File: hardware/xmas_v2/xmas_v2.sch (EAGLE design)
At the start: 30 parts

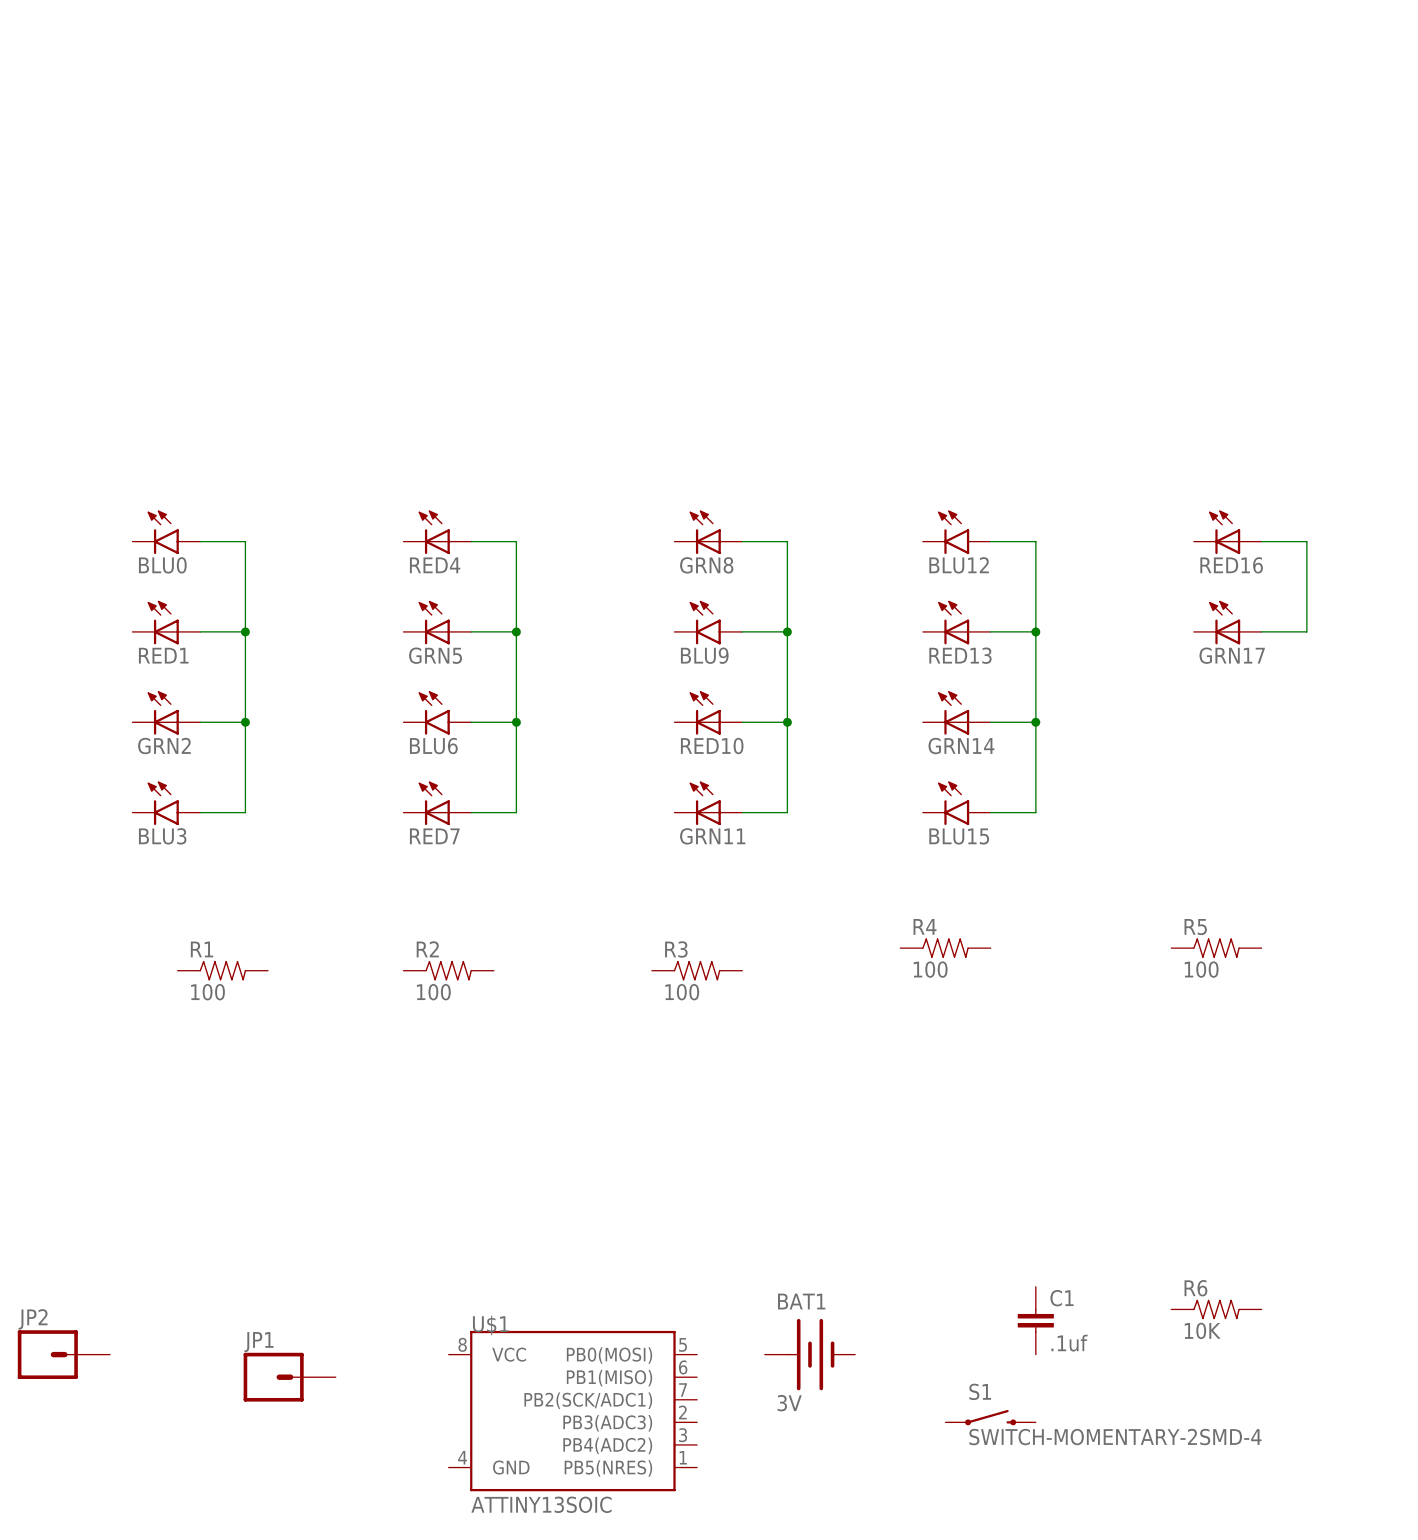
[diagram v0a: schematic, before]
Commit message: Added charlieplex schem
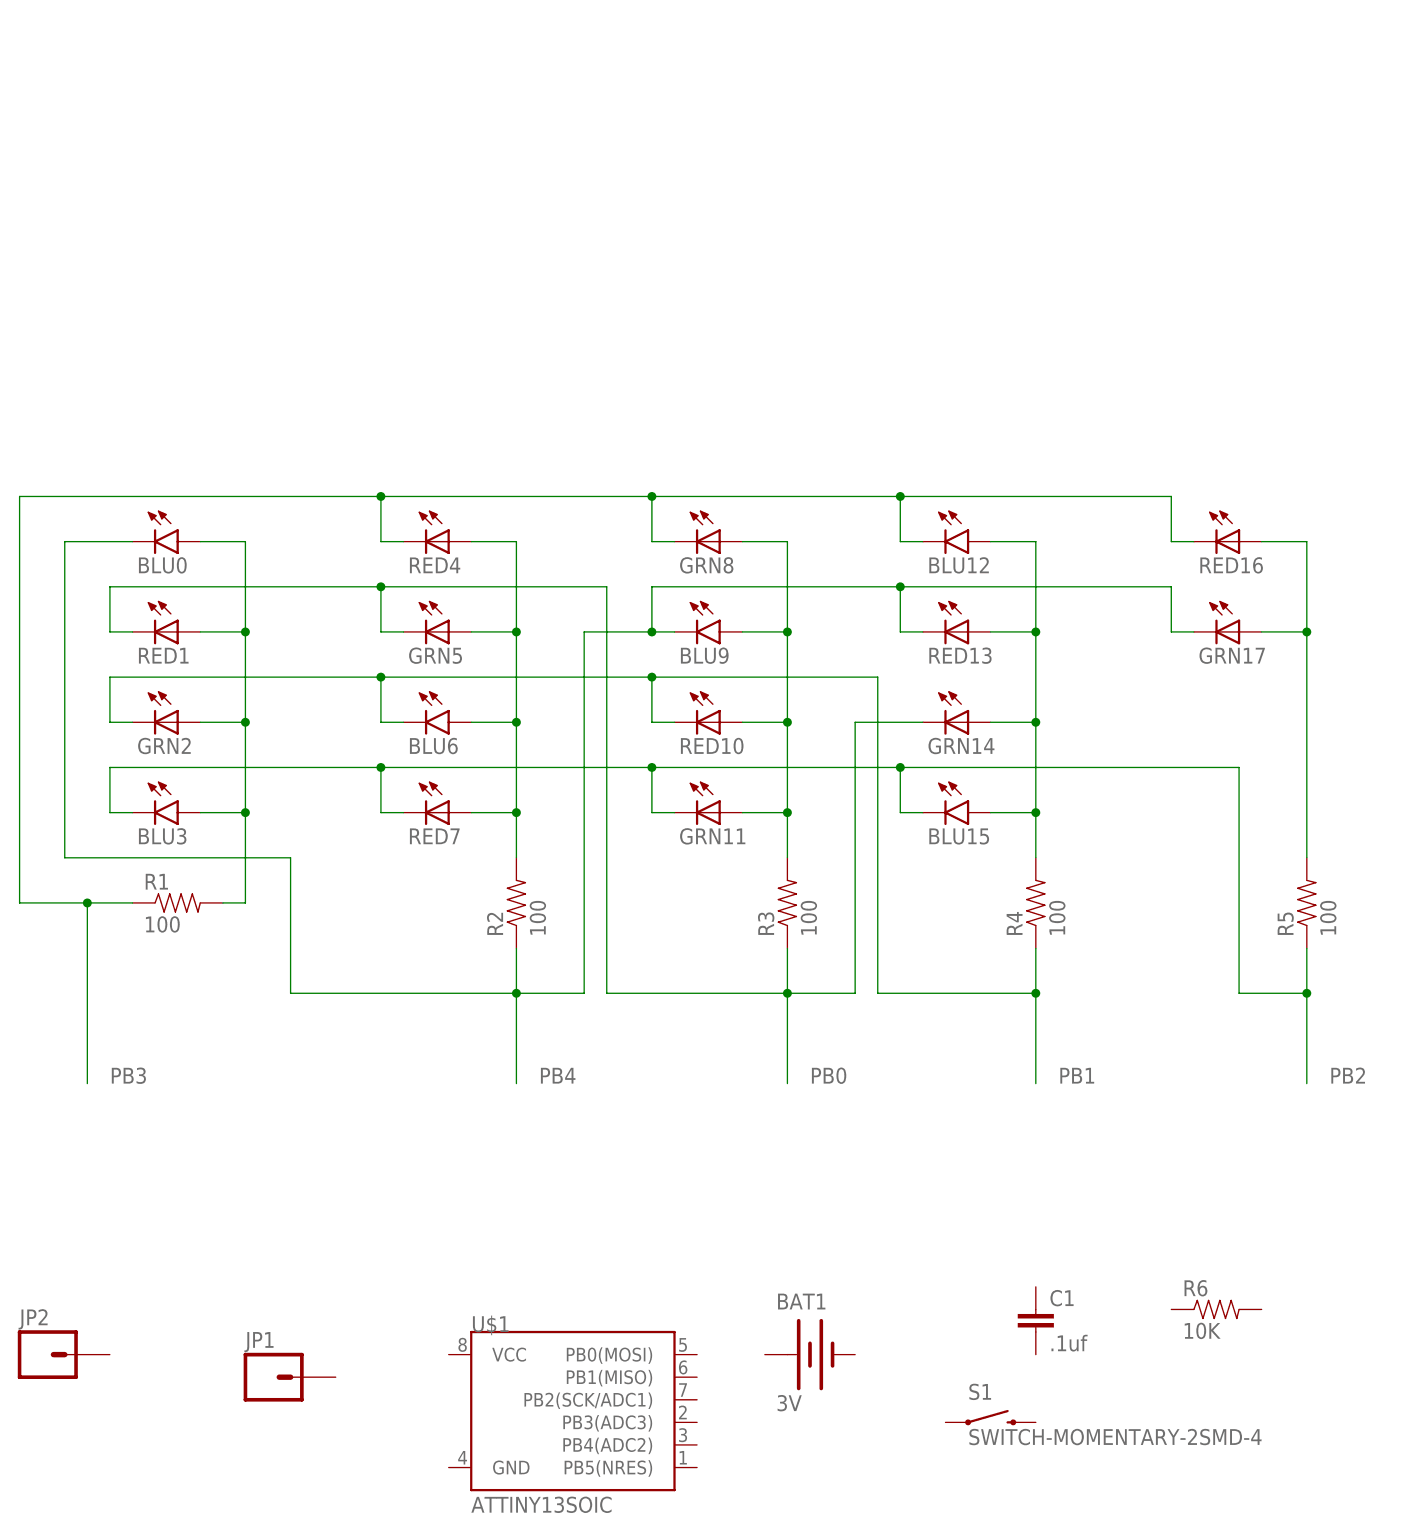
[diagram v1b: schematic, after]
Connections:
- new net N$1: BLU0.A, BLU3.A, GRN2.A, R1.2, RED1.A
- new net N$2: BLU6.A, GRN5.A, R2.2, RED4.A, RED7.A
- new net N$3: BLU9.A, GRN11.A, GRN8.A, R3.2, RED10.A
- new net N$4: BLU12.A, BLU15.A, GRN14.A, R4.2, RED13.A
- new net N$5: GRN17.A, R5.2, RED16.A
- net PB0: now also GRN14.C, GRN5.C, R3.1, RED1.C; no longer BLU9.A, GRN11.A, GRN8.A, RED10.A
- net PB1: now also BLU6.C, GRN2.C, R4.1, RED10.C; no longer BLU12.A, BLU15.A, GRN14.A, RED13.A
- net PB2: now also BLU15.C, BLU3.C, GRN11.C, R5.1, RED7.C; no longer GRN17.A, RED16.A
- net PB3: now also BLU12.C, GRN8.C, R1.1, RED16.C, RED4.C; no longer BLU0.A, BLU3.A, GRN2.A, RED1.A
- net PB4: now also BLU0.C, BLU9.C, GRN17.C, R2.1, RED13.C; no longer BLU6.A, GRN5.A, RED4.A, RED7.A
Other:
- moved on the sheet: R1, R2, R3, R4, R5

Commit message: Schematic is done
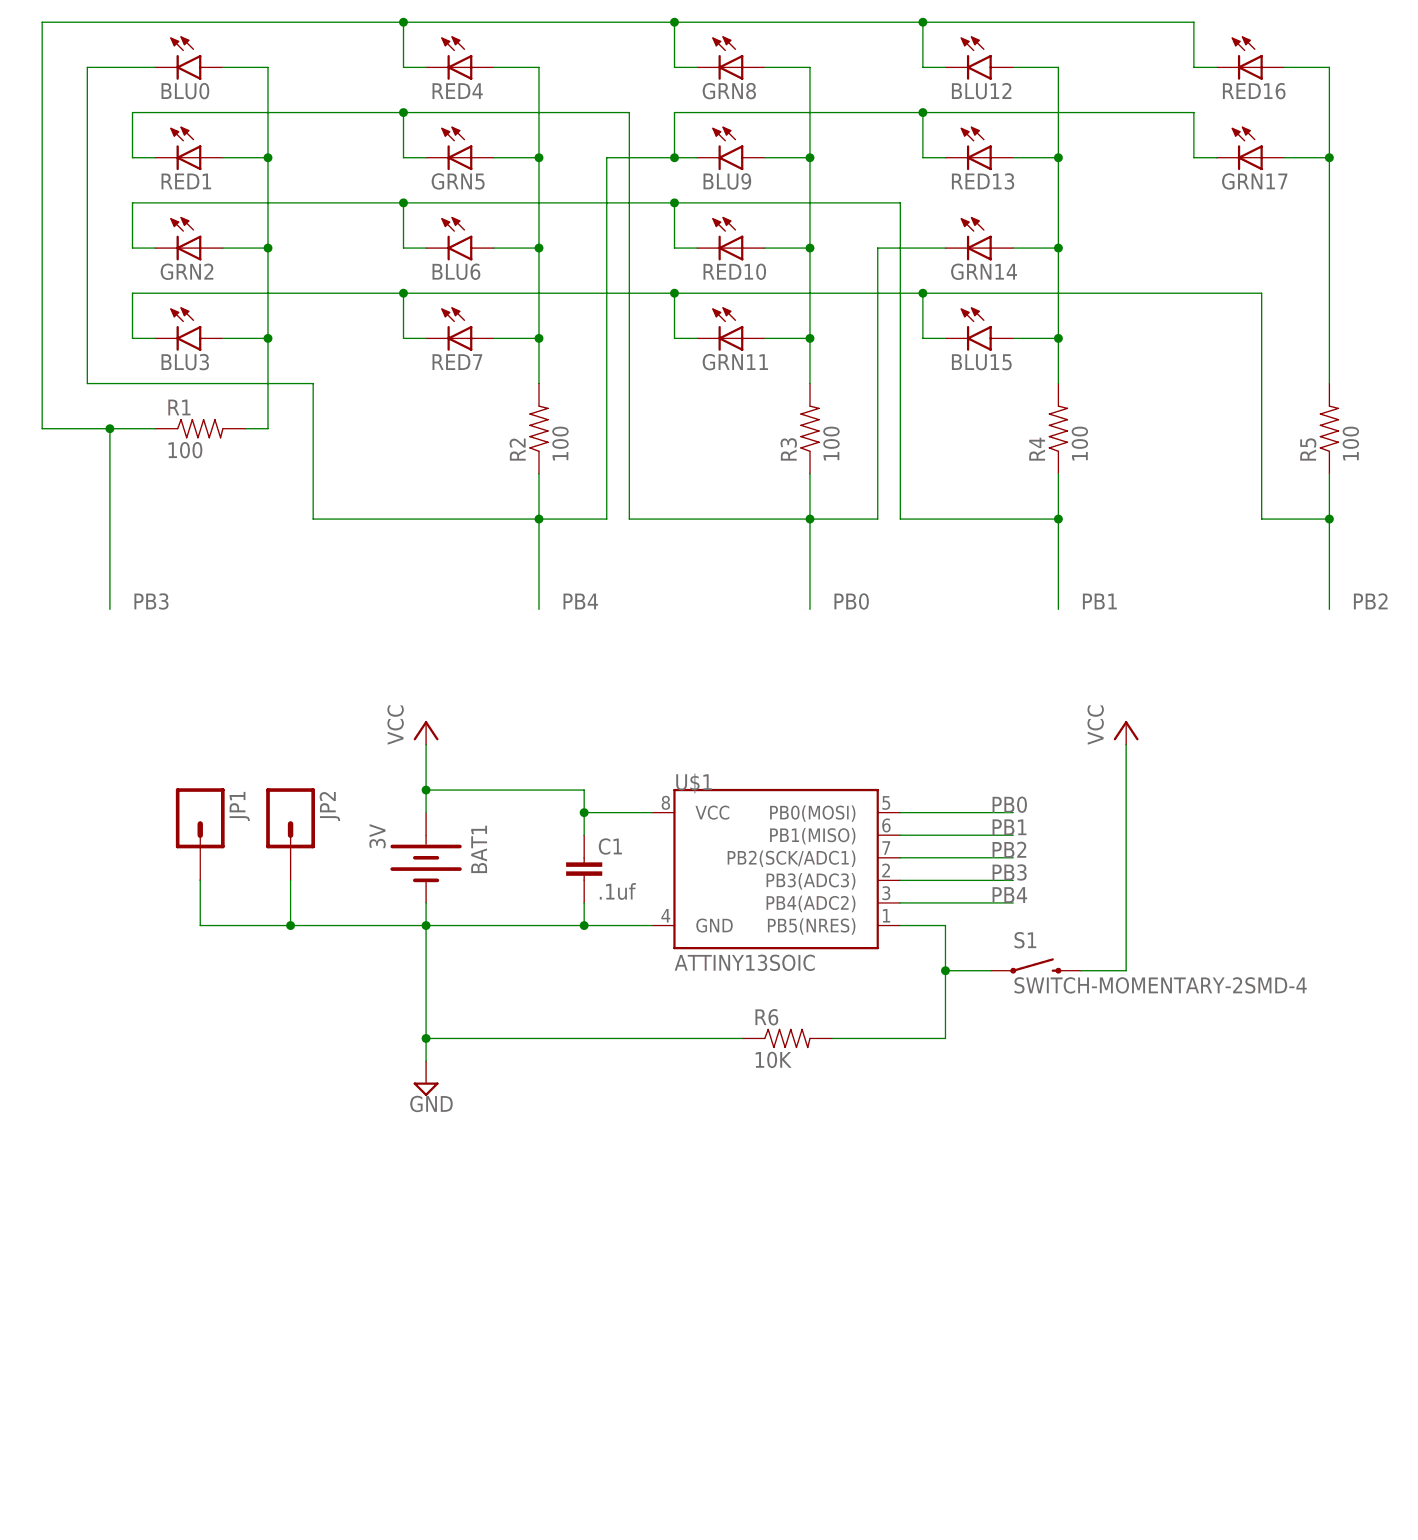
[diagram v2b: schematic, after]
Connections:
- new net GND: BAT1.-, C1.2, JP1.1, JP2.1, R6.1, U$1.GND
- new net N$10: R6.2, S1.1, U$1.PB5(NRES)
- new net VCC: BAT1.+, C1.1, S1.2, U$1.VCC
- net PB0: now also U$1.PB0(MOSI)
- net PB1: now also U$1.PB1(MISO)
- net PB2: now also U$1.PB2(SCK/ADC1)
- net PB3: now also U$1.PB3(ADC3)
- net PB4: now also U$1.PB4(ADC2)
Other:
- moved on the sheet: BAT1, BLU0, BLU12, BLU15, BLU3, BLU6, BLU9, C1, GRN11, GRN14, GRN17, GRN2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

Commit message: Finished routing
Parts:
- BLU0: value (none) -> 0
- BLU12: value (none) -> 12
- BLU15: value (none) -> 15
- BLU3: value (none) -> 3
- BLU6: value (none) -> 6
- BLU9: value (none) -> 9
- GRN11: value (none) -> 11
- GRN14: value (none) -> 14
- GRN17: value (none) -> 17
- GRN2: value (none) -> 2
- GRN5: value (none) -> 5
- GRN8: value (none) -> 8
- RED1: value (none) -> 1
- RED10: value (none) -> 10
- RED13: value (none) -> 13
- RED16: value (none) -> 16
- RED4: value (none) -> 4
- RED7: value (none) -> 7
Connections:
- net GND: no longer JP1.1, JP2.1
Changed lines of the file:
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@@
 <parts>
 <part name="U$1" library="SparkFun-DigitalIC" deviceset="ATTINY13" device="SOIC"/>
-<part name="BLU0" library="SparkFun-LED" deviceset="LED" device="5MM-KIT"/>
-<part name="BLU3" library="SparkFun-LED" deviceset="LED" device="5MM-KIT"/>
-<part name="BLU6" library="SparkFun-LED" deviceset="LED" device="5MM-KIT"/>
-<part name="BLU9" library="SparkFun-LED" deviceset="LED" device="5MM-KIT"/>
-<part name="BLU12" library="SparkFun-LED" deviceset="LED" device="5MM-KIT"/>
-<part name="BLU15" library="SparkFun-LED" deviceset="LED" device="5MM-KIT"/>
-<part name="RED1" library="adafruit" deviceset="LED" device="CHIPLED_0805"/>
-<part name="RED4" library="adafruit" deviceset="LED" device="CHIPLED_0805"/>
-<part name="RED7" library="adafruit" deviceset="LED" device="CHIPLED_0805"/>
-<part name="RED10" library="adafruit" deviceset="LED" device="CHIPLED_0805"/>
-<part name="RED13" library="adafruit" deviceset="LED" device="CHIPLED_0805"/>
-<part name="RED16" library="adafruit" deviceset="LED" device="CHIPLED_0805"/>
-<part name="GRN2" library="adafruit" deviceset="LED" device="CHIPLED_0805"/>
-<part name="GRN5" library="adafruit" deviceset="LED" device="CHIPLED_0805"/>
-<part name="GRN8" library="adafruit" deviceset="LED" device="CHIPLED_0805"/>
-<part name="GRN11" library="adafruit" deviceset="LED" device="CHIPLED_0805"/>
-<part name="GRN14" library="adafruit" deviceset="LED" device="CHIPLED_0805"/>
-<part name="GRN17" library="adafruit" deviceset="LED" device="CHIPLED_0805"/>
+<part name="BLU0" library="SparkFun-LED" deviceset="LED" device="5MM-KIT" value="0"/>
+<part name="BLU3" library="SparkFun-LED" deviceset="LED" device="5MM-KIT" value="3"/>
+<part name="BLU6" library="SparkFun-LED" deviceset="LED" device="5MM-KIT" value="6"/>
+<part name="BLU9" library="SparkFun-LED" deviceset="LED" device="5MM-KIT" value="9"/>
+<part name="BLU12" library="SparkFun-LED" deviceset="LED" device="5MM-KIT" value="12"/>
+<part name="BLU15" library="SparkFun-LED" deviceset="LED" device="5MM-KIT" value="15"/>
+<part name="RED1" library="adafruit" deviceset="LED" device="CHIPLED_0805" value="1"/>
+<part name="RED4" library="adafruit" deviceset="LED" device="CHIPLED_0805" value="4"/>
+<part name="RED7" library="adafruit" deviceset="LED" device="CHIPLED_0805" value="7"/>
+<part name="RED10" library="adafruit" deviceset="LED" device="CHIPLED_0805" value="10"/>
+<part name="RED13" library="adafruit" deviceset="LED" device="CHIPLED_0805" value="13"/>
+<part name="RED16" library="adafruit" deviceset="LED" device="CHIPLED_0805" value="16"/>
+<part name="GRN2" library="adafruit" deviceset="LED" device="CHIPLED_0805" value="2"/>
+<part name="GRN5" library="adafruit" deviceset="LED" device="CHIPLED_0805" value="5"/>
+<part name="GRN8" library="adafruit" deviceset="LED" device="CHIPLED_0805" value="8"/>
+<part name="GRN11" library="adafruit" deviceset="LED" device="CHIPLED_0805" value="11"/>
+<part name="GRN14" library="adafruit" deviceset="LED" device="CHIPLED_0805" value="14"/>
+<part name="GRN17" library="adafruit" deviceset="LED" device="CHIPLED_0805" value="17"/>
 <part name="BAT1" library="SparkFun-Electromechanical" deviceset="BATTERY" device="20PTH" value="3V"/>
 <part name="S1" library="SparkFun-Electromechanical" deviceset="SWITCH-MOMENTARY-2" device="SMD-4"/>
@@
 <wire x1="50.8" y1="25.4" x2="50.8" y2="12.7" width="0.1524" layer="91"/>
 <junction x="50.8" y="25.4"/>
-<pinref part="JP2" gate="G$1" pin="1"/>
 <wire x1="50.8" y1="12.7" x2="50.8" y2="10.16" width="0.1524" layer="91"/>
-<wire x1="50.8" y1="25.4" x2="35.56" y2="25.4" width="0.1524" layer="91"/>
-<wire x1="35.56" y1="25.4" x2="35.56" y2="30.48" width="0.1524" layer="91"/>
-<pinref part="JP1" gate="G$1" pin="1"/>
-<wire x1="35.56" y1="25.4" x2="25.4" y2="25.4" width="0.1524" layer="91"/>
-<wire x1="25.4" y1="25.4" x2="25.4" y2="30.48" width="0.1524" layer="91"/>
-<junction x="35.56" y="25.4"/>
 <pinref part="R6" gate="G$1" pin="1"/>
 <wire x1="86.36" y1="12.7" x2="50.8" y2="12.7" width="0.1524" layer="91"/>
